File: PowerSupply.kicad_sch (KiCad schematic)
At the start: 32 parts, among them J901 U.FL-R-SMT(10), J902 U.FL-R-SMT(10), J903 U.FL-R-SMT(10), J904 U.FL-R-SMT(10), J905 U.FL-R-SMT(10), J906 U.FL-R-SMT(10), U901 BAT54W-7-F, U902 ZXCT1009QFTA, U903 LT6233CS6#TRMPBF

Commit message: Updates from Michal to fix ERC errors
Still lots of ERC warnings
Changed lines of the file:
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@@
 	(wire
 		(pts
-			(xy 347.98 96.52) (xy 335.28 96.52)
+			(xy 335.28 96.52) (xy 347.98 96.52)
 		)
 		(stroke

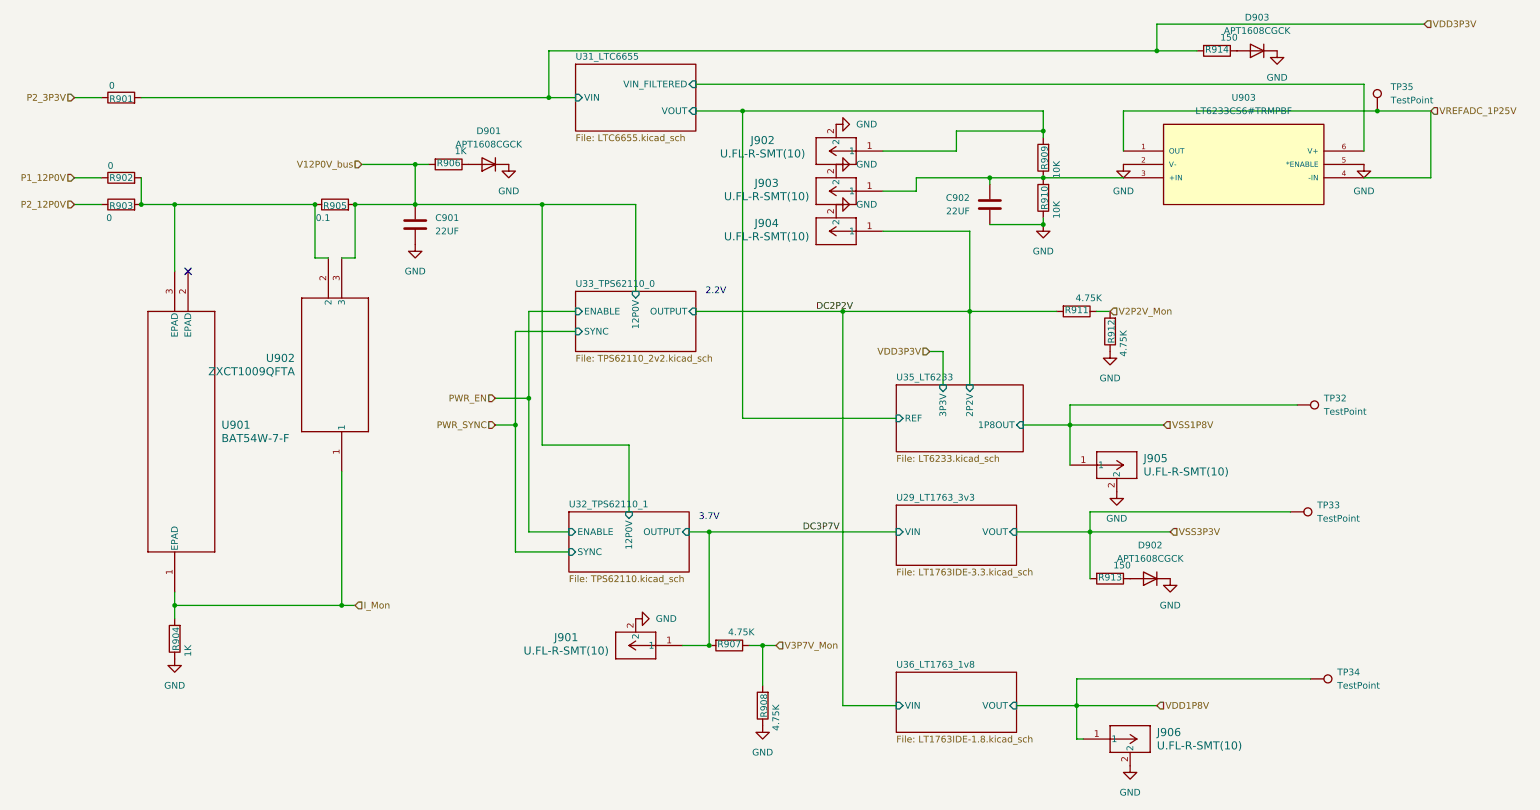
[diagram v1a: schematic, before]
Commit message: Schematic Changes
Added Manufacturer/MPN/Description Fields to parts
Added libraries to project
Modified FMC schematic to use new symbol
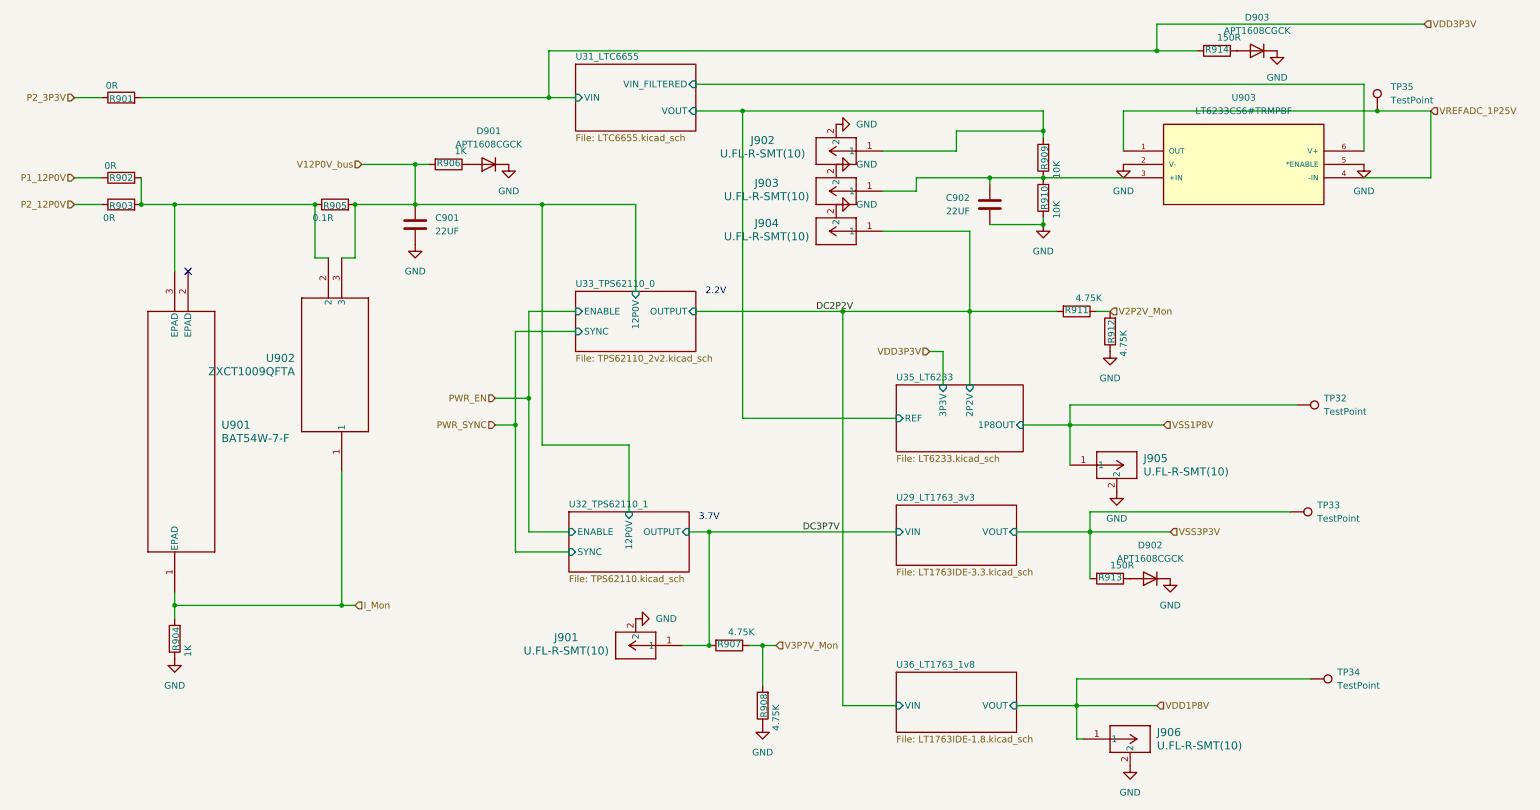
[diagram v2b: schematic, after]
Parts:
- C901: Manufacturer (none) -> Murata; Manufacturer Part Number (none) -> GRM31CR61E226KE15L
- C902: Manufacturer (none) -> Panasonic; Manufacturer Part Number (none) -> EEF-CD1B220R
- D901, D902, D903: Manufacturer (none) -> Kingbright; Manufacturer Part Number (none) -> APT1608CGCK
- J901, J902, J903, J904, J905, J906: Manufacturer (none) -> Hirose; Manufacturer Part Number (none) -> U.FL-R-SMT(10)
- R901, R902, R903: value 0 -> 0R; Manufacturer (none) -> Panasonic; Manufacturer Part Number (none) -> ERJ-3GEY0R00V
- R904, R906: Manufacturer (none) -> YAGEO; Manufacturer Part Number (none) -> RC0603FR-071KL
- R905: value 0.1 -> 0.1R; Manufacturer (none) -> Samsung; Manufacturer Part Number (none) -> RUW3216FR100CS
- R907, R908, R911, R912: Manufacturer (none) -> YAGEO; Manufacturer Part Number (none) -> RC0603FR-074K75L
- R909, R910: Manufacturer (none) -> Vishay; Manufacturer Part Number (none) -> MCT0603MD1002DP500
- R913, R914: value 150 -> 150R; Manufacturer (none) -> YAGEO; Manufacturer Part Number (none) -> RC0603FR-07150RL
- U901: Manufacturer (none) -> Diodes Incorporated; Manufacturer Part Number (none) -> BAT54W-7-F
- U902: Manufacturer (none) -> Diodes Incorporated; Manufacturer Part Number (none) -> ZXCT1009QFTA
- U903: Manufacturer (none) -> Analog Devices; Manufacturer Part Number (none) -> LT6233CS6#TRMPBF

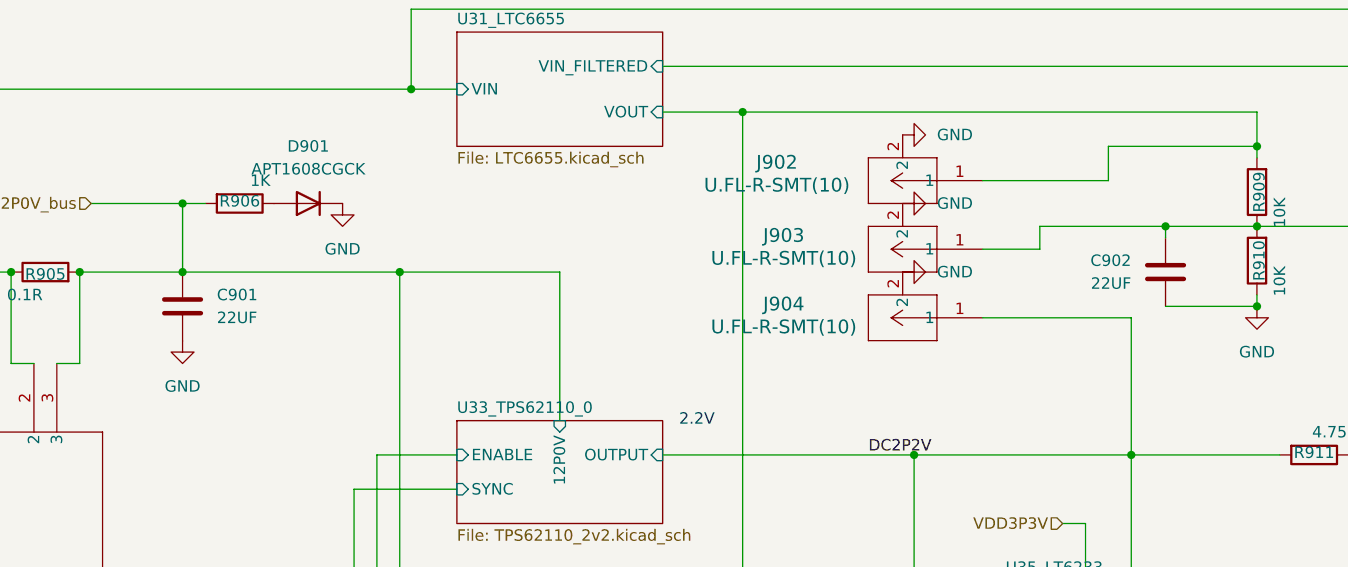
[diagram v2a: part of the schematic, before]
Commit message: Schematics update
Cleaned up RF ADC and front end sections.
Verified that changes did not changes anything about the layout.
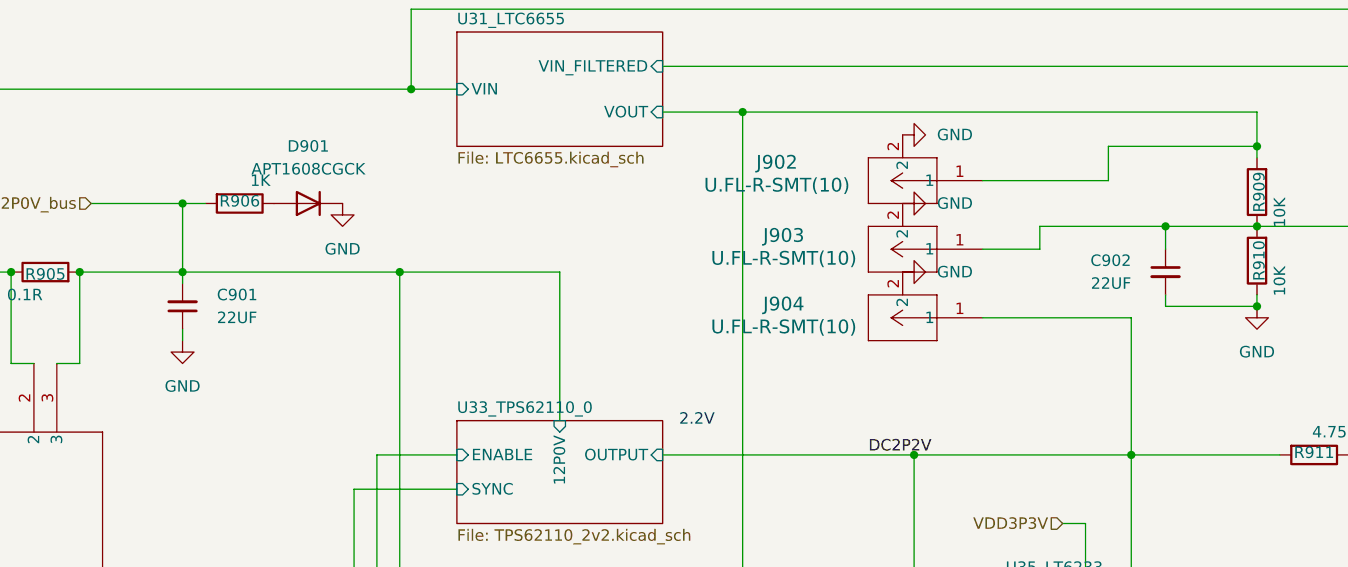
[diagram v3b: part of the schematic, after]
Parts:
- C901, C902: symbol Device:C -> Device:C_Small
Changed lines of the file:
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@@
 	(wire
 		(pts
+			(xy 154.94 107.95) (xy 154.94 109.22)
+		)
+		(stroke
+			(width 0)
+			(type default)
+		)
+	)
+	(wire
+		(pts
 			(xy 289.56 83.82) (xy 337.82 83.82)
 		)
@@
 	(wire
 		(pts
-			(xy 264.16 96.52) (xy 264.16 97.79)
+			(xy 264.16 96.52) (xy 264.16 99.06)
+		)
+		(stroke
+			(width 0)
+			(type default)
+		)
+	)
+	(wire
+		(pts
+			(xy 154.94 101.6) (xy 154.94 102.87)
 		)
 		(stroke
@@
 	(wire
 		(pts
+			(xy 264.16 104.14) (xy 264.16 105.41)
+		)
+		(stroke
+			(width 0)
+			(type default)
+		)
+	)
+	(wire
+		(pts
 			(xy 236.22 121.92) (xy 260.35 121.92)
 		)
@@
 	)
 	(symbol
-		(lib_id "Device:C")
+		(lib_id "Device:C_Small")
 		(at 264.16 101.6 0)
 		(mirror y)
@@
 	)
 	(symbol
-		(lib_id "Device:C")
+		(lib_id "Device:C_Small")
 		(at 154.94 105.41 180)
 		(unit 1)

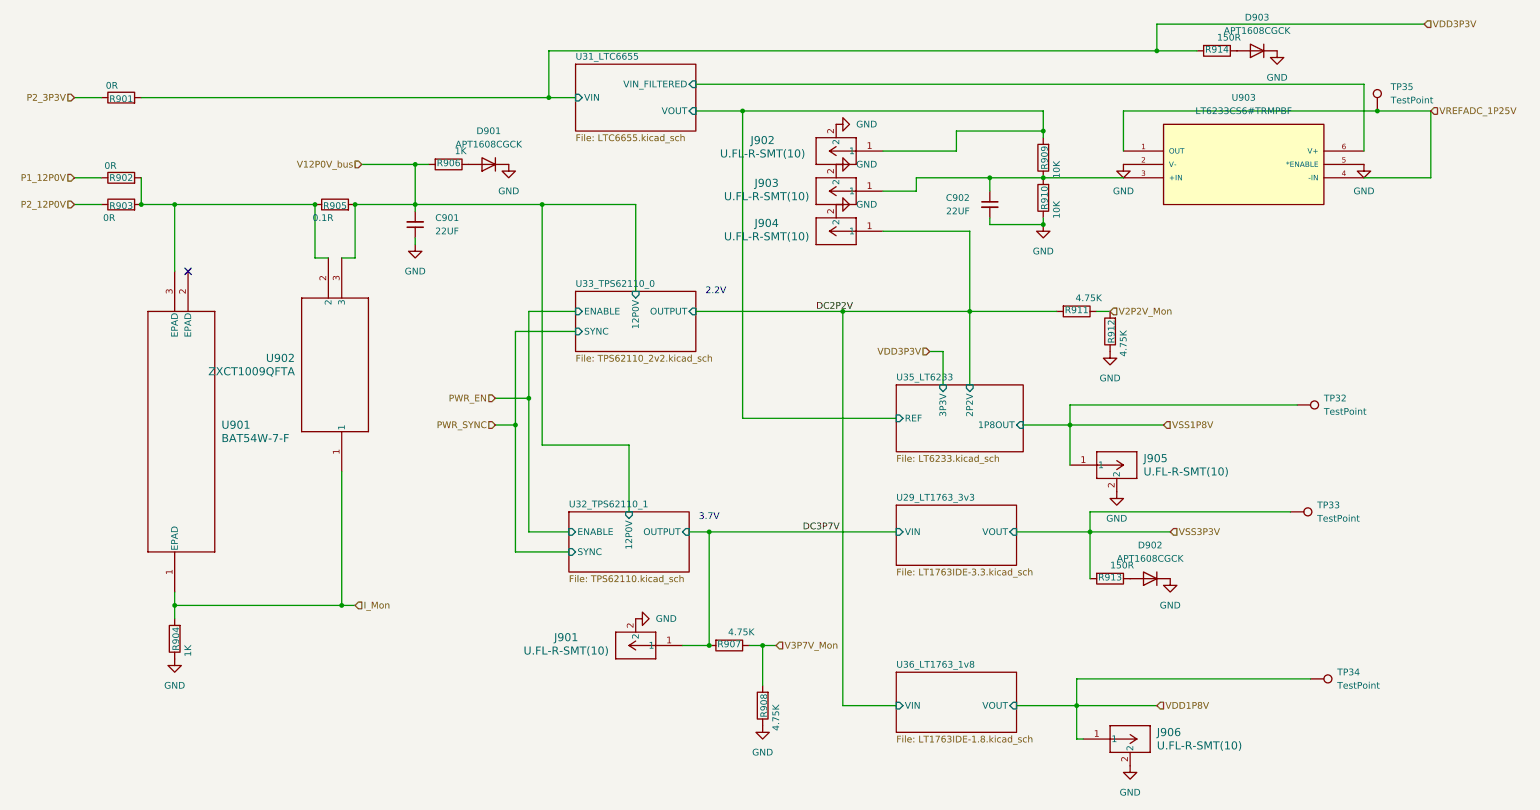
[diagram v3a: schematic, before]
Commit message: Updated some Schematics
- updated slowmon schematic
- updated diff to se schematic
- cleaned up DRC/ERC errors
No changes were made that effected the PCB layout
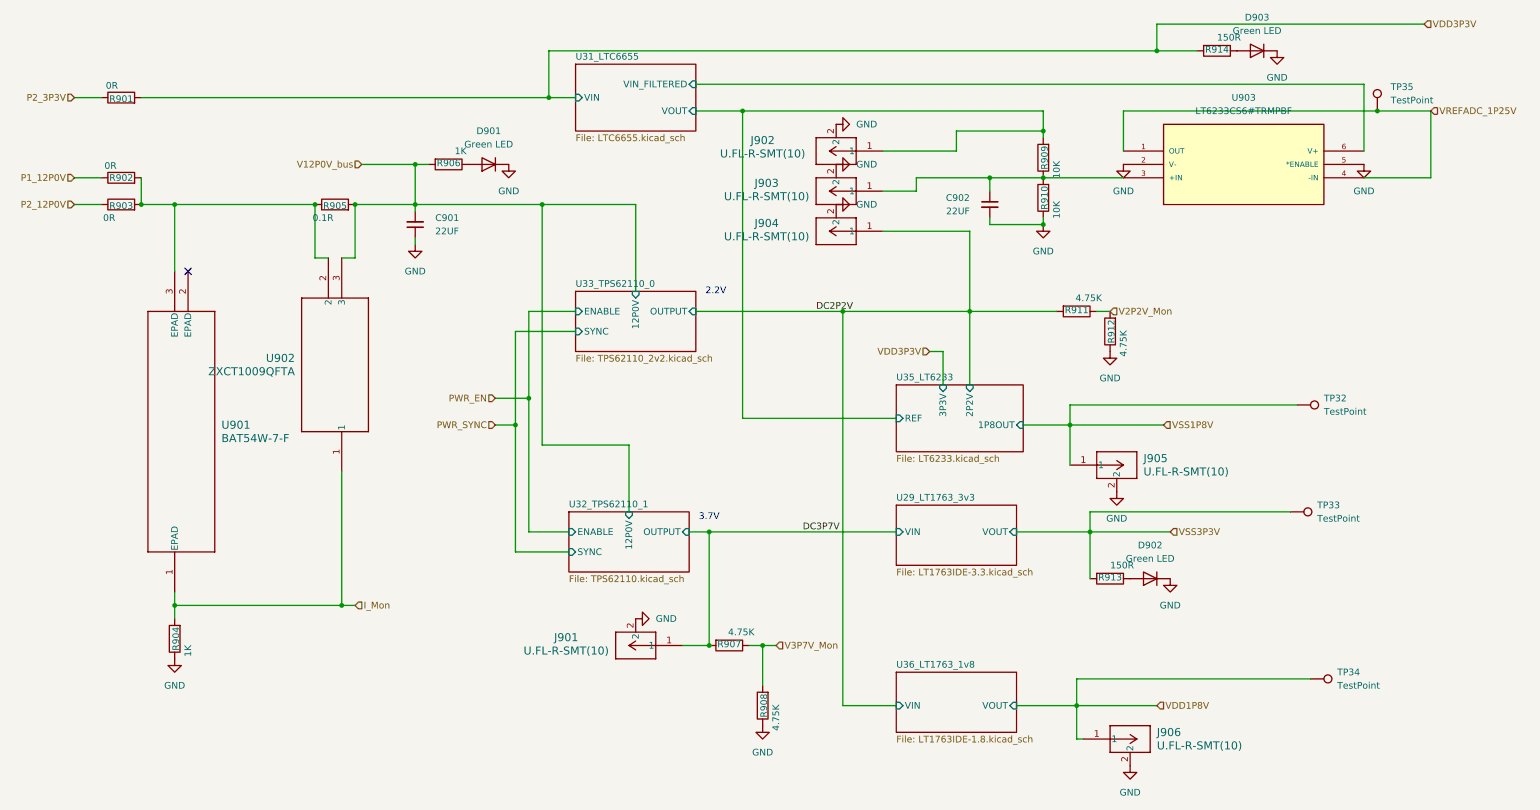
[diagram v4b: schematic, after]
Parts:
- D901, D902, D903: value APT1608CGCK -> Green LED
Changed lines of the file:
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@@
 			)
 		)
-		(property "Value" "APT1608CGCK"
+		(property "Value" "Green LED"
 			(at 168.91 90.17 0)
 			(effects
@@
 			)
 		)
-		(property "Value" "APT1608CGCK"
+		(property "Value" "Green LED"
 			(at 314.96 68.58 0)
 			(effects
@@
 			)
 		)
-		(property "Value" "APT1608CGCK"
+		(property "Value" "Green LED"
 			(at 294.64 168.91 0)
 			(effects
